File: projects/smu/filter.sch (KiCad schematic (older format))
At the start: 6 parts, among them U600 LM13700, U601 LM741

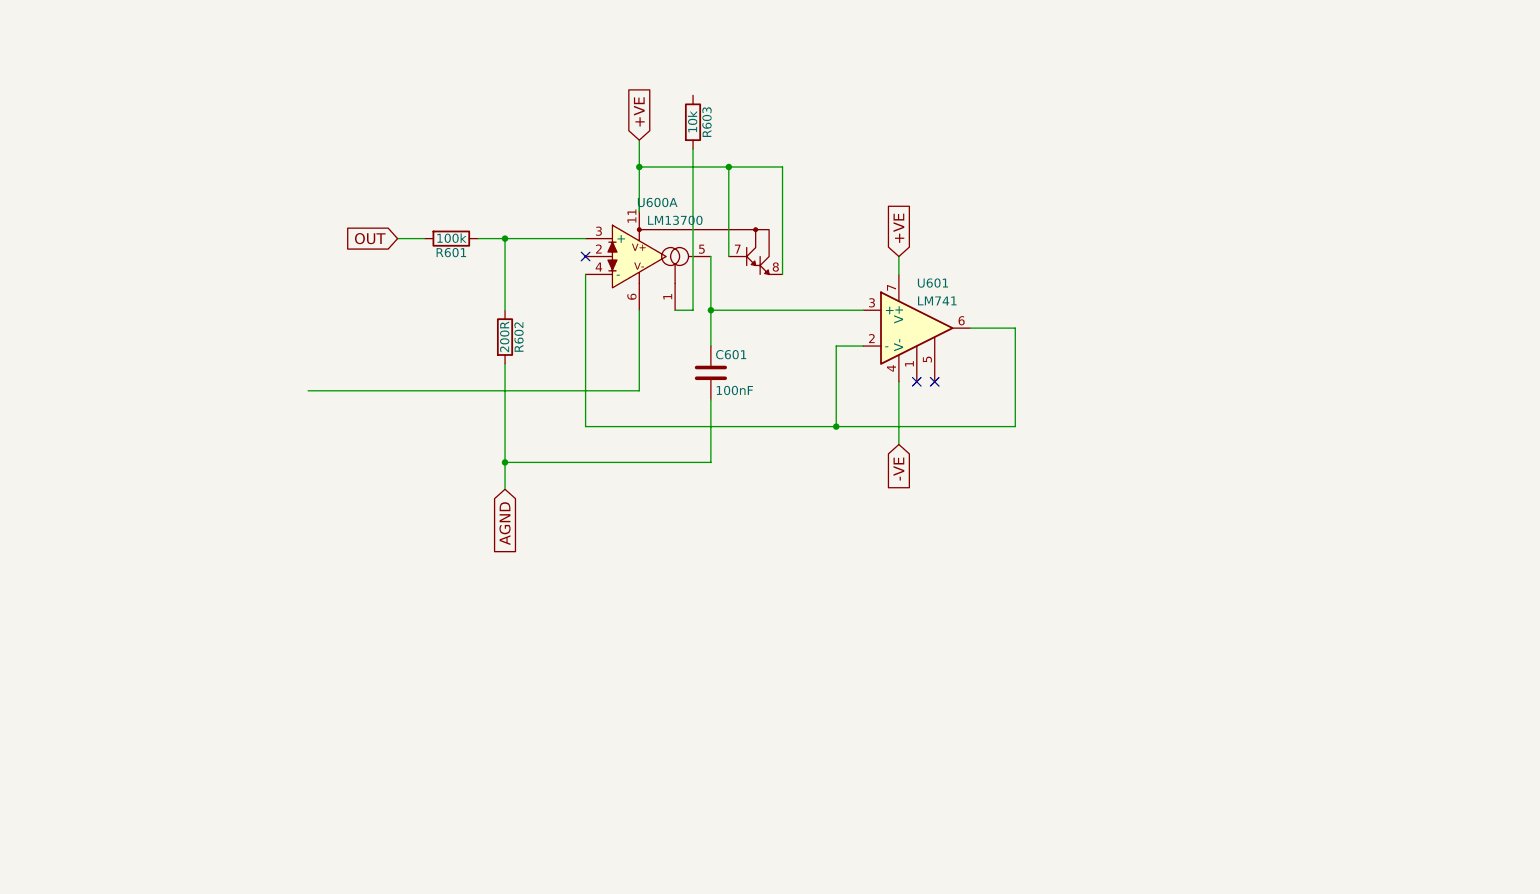
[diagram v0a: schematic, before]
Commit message: add output section
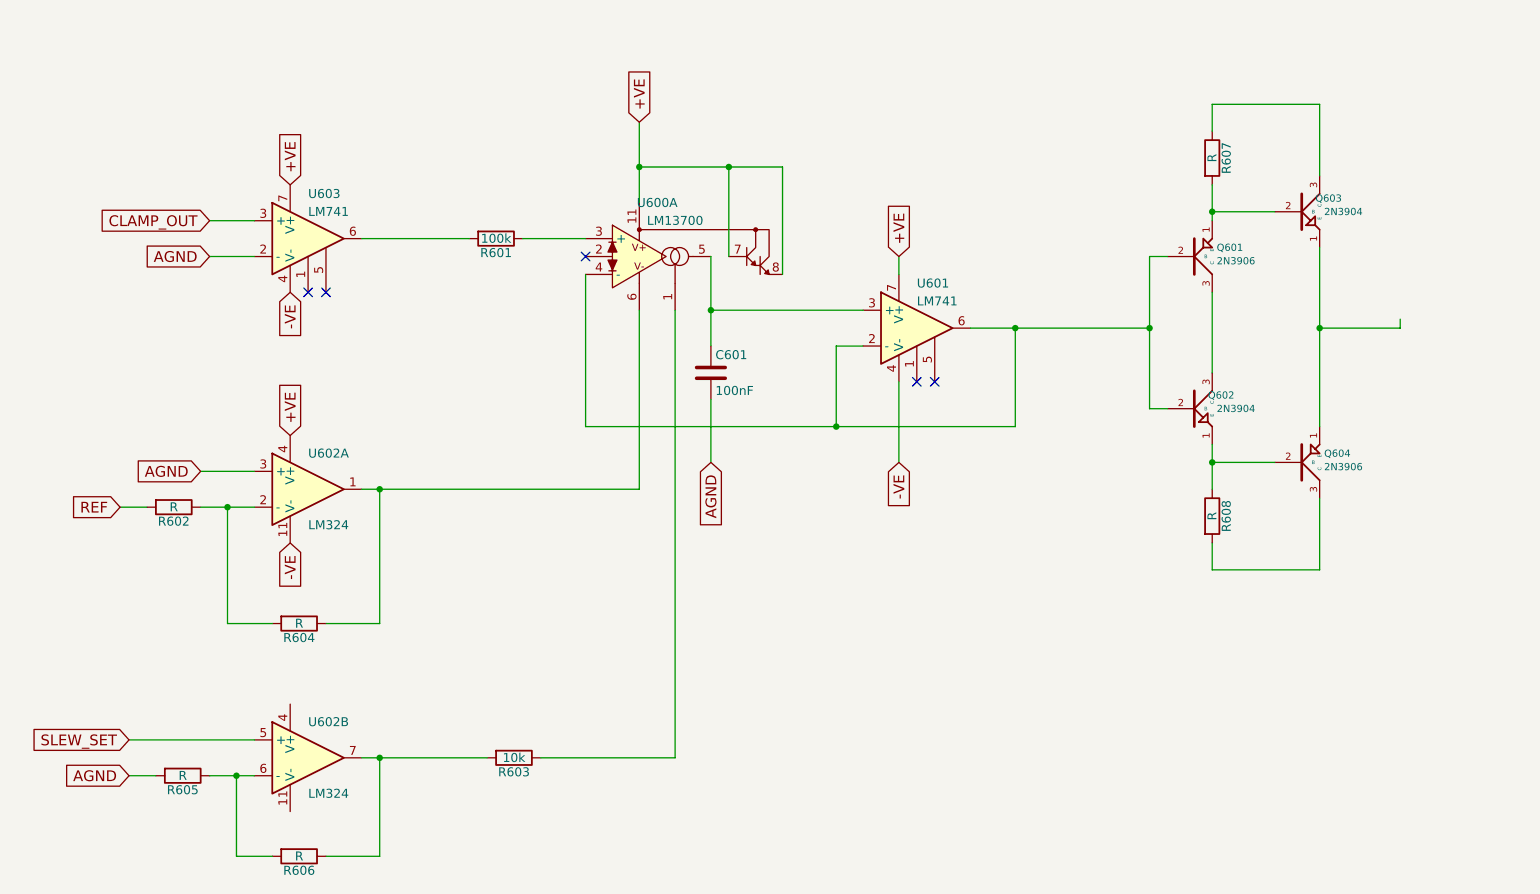
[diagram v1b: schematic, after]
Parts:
- added Q601, Q604: 2N3906, symbol 2N3906
- added Q602, Q603: 2N3904, symbol 2N3904
- added R604, R605, R606, R607, R608: R, symbol R
- added U602: LM324, symbol LM324
- added U603: LM741, symbol LM741
- R602: value 200R -> R
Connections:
- net labels added: CLAMP_OUT, REF, SLEW_SET
- net labels removed: OUT
- wire segments 24 -> 55
- no-connect marks 3 -> 5
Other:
- moved on the sheet: R601, R603

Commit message: update
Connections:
- net OUT: now reaches Q603.1 (E), Q604.1 (E)
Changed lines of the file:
@@
 $Descr A4 11693 8268
 encoding utf-8
-Sheet 6 6
+Sheet 6 7
 Title ""
 Date ""
@@
 Wire Wire Line
 	8150 3400 8600 3400
-Wire Wire Line
-	8600 3400 8600 3350
 Connection ~ 8150 3400
 Wire Wire Line
@@
 Wire Wire Line
 	8150 4750 8150 4350
+Text GLabel 8600 3400 2    60   Input ~ 0
+OUT
 $EndSCHEMATC

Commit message: add schematic for relay
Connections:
- net +VE: now also Q603.3 (C), R607.1
- net -VE: now also Q604.3 (C), R608.2
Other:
- note added: "we can control the current resistors with mosfets \nif we really want - or even a VtoI converter\n\n"
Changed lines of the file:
@@
 	4850 3000 4850 2500
 Wire Wire Line
-	4350 2500 5150 2500
+	4350 2500 4850 2500
+Wire Wire Line
+	4850 2500 5150 2500
 Wire Wire Line
 	5150 2500 5150 3100
@@
 $EndComp
 Wire Wire Line
-	4750 3000 4750 3500
+	4750 3000 4750 3300
+Wire Wire Line
+	4750 3300 4750 3500
 Wire Wire Line
 	4750 3300 5600 3300
@@
 $EndComp
 Wire Wire Line
-	6200 3400 7200 3400
+	6200 3400 6450 3400
+Wire Wire Line
+	6450 3400 7200 3400
 Wire Wire Line
 	6450 3950 6450 3400
@@
 	4050 3100 4050 3950
 Wire Wire Line
-	4050 3950 6450 3950
+	4050 3950 5450 3950
+Wire Wire Line
+	5450 3950 6450 3950
 Text GLabel 4750 4150 3    60   Input ~ 0
 AGND
@@
 NoConn ~ 6000 3700
 Wire Wire Line
-	4350 2250 4350 2700
+	4350 2250 4350 2500
+Wire Wire Line
+	4350 2500 4350 2700
 Wire Wire Line
 	4350 4300 4350 3300
@@
 $EndComp
 Wire Wire Line
-	2800 4300 4350 4300
+	2800 4300 2900 4300
+Wire Wire Line
+	2900 4300 4350 4300
 $Comp
 L R R604
@@
 $EndComp
 Wire Wire Line
-	1900 4400 2200 4400
+	1900 4400 2050 4400
+Wire Wire Line
+	2050 4400 2200 4400
 Wire Wire Line
 	2050 4400 2050 5050
@@
 	4550 3300 4550 5800
 Wire Wire Line
-	2800 5800 3500 5800
+	2800 5800 2900 5800
+Wire Wire Line
+	2900 5800 3500 5800
 Wire Wire Line
 	4550 5800 3800 5800
@@
 	2100 6350 2100 5900
 Wire Wire Line
-	1950 5900 2200 5900
+	1950 5900 2100 5900
+Wire Wire Line
+	2100 5900 2200 5900
 Connection ~ 2100 5900
 Wire Wire Line
@@
 	7550 3200 7550 3650
 Wire Wire Line
-	7200 3000 7200 3850
+	7200 3000 7200 3400
+Wire Wire Line
+	7200 3400 7200 3850
 Wire Wire Line
 	7200 3000 7300 3000
@@
 $EndComp
 Wire Wire Line
-	7550 2600 7550 2800
+	7550 2600 7550 2750
+Wire Wire Line
+	7550 2750 7550 2800
 $Comp
 L 2N3904 Q603
@@
 $EndComp
 Wire Wire Line
-	8150 2950 8150 3950
+	8150 2950 8150 3400
+Wire Wire Line
+	8150 3400 8150 3950
 $Comp
 L R R608
@@
 $EndComp
 Wire Wire Line
-	7550 4050 7550 4300
+	7550 4050 7550 4150
+Wire Wire Line
+	7550 4150 7550 4300
 Wire Wire Line
 	7900 4150 7550 4150
@@
 Connection ~ 8150 3400
 Wire Wire Line
-	8150 2550 8150 2150
+	8150 2000 8150 2150
+Wire Wire Line
+	8150 2150 8150 2550
 Wire Wire Line
 	8150 2150 7550 2150
@@
 	7550 4750 8150 4750
 Wire Wire Line
-	8150 4750 8150 4350
+	8150 4350 8150 4750
+Wire Wire Line
+	8150 4750 8150 4900
 Text GLabel 8600 3400 2    60   Input ~ 0
 OUT
+Text GLabel 8150 2000 1    60   Input ~ 0
++VE
+Connection ~ 8150 2150
+Text GLabel 8150 4900 3    60   Input ~ 0
+-VE
+Connection ~ 8150 4750
+Text Notes 6500 2300 0    60   ~ 0
+we can control the current resistors with mosfets \nif we really want - or even a VtoI converter\n\n
 $EndSCHEMATC
